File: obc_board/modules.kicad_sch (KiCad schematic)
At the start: 26 parts, among them J1 FSI-110-03-X-D-AD-SD-K-TR, J2 FSI-110-03-X-D-AD-SD-K-TR, U12 LTC4304IMS#PBF, U13 LTC4304IMS#PBF

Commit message: updated pcb
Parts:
- FL1, FL2: footprint FIL_PLT5BPH1015R6SNL -> cubesat_obc:FIL_PLT5BPH1015R6SNL
- J1, J2: footprint SAMTEC_FSI-110-03-X-D-AD-SD-K-TR -> cubesat_obc:SAMTEC_FSI-110-10-X-D-AD-TR
- U12, U13: footprint MSOP-10_MS -> Package_SO:MSOP-10_3x3mm_P0.5mm
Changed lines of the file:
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@@
     (property "Reference" "J1" (id 0) (at 115.57 56.7182 0))
     (property "Value" "FSI-110-03-X-D-AD-SD-K-TR" (id 1) (at 115.57 59.0296 0))
-    (property "Footprint" "SAMTEC_FSI-110-03-X-D-AD-SD-K-TR" (id 2) (at 115.57 76.2 0)
+    (property "Footprint" "cubesat_obc:SAMTEC_FSI-110-10-X-D-AD-TR" (id 2) (at 115.57 76.2 0)
       (effects (font (size 1.27 1.27)) (justify left bottom) hide)
     )
@@
     (property "Reference" "FL1" (id 0) (at 68.58 52.9082 0))
     (property "Value" "PLT5BPH1015R6SNL" (id 1) (at 68.58 55.2196 0))
-    (property "Footprint" "FIL_PLT5BPH1015R6SNL" (id 2) (at 68.58 63.5 0)
+    (property "Footprint" "cubesat_obc:FIL_PLT5BPH1015R6SNL" (id 2) (at 68.58 63.5 0)
       (effects (font (size 1.27 1.27)) (justify left bottom) hide)
     )
@@
     (property "Reference" "U12" (id 0) (at 93.98 98.6282 0))
     (property "Value" "LTC4304IMS#PBF" (id 1) (at 93.98 100.9396 0))
-    (property "Footprint" "MSOP-10_MS" (id 2) (at 78.74 105.41 0)
+    (property "Footprint" "Package_SO:MSOP-10_3x3mm_P0.5mm" (id 2) (at 78.74 105.41 0)
       (effects (font (size 1.27 1.27)) (justify left bottom) hide)
     )
@@
     (property "Reference" "J2" (id 0) (at 224.79 56.7182 0))
     (property "Value" "FSI-110-03-X-D-AD-SD-K-TR" (id 1) (at 224.79 59.0296 0))
-    (property "Footprint" "SAMTEC_FSI-110-03-X-D-AD-SD-K-TR" (id 2) (at 224.79 76.2 0)
+    (property "Footprint" "cubesat_obc:SAMTEC_FSI-110-10-X-D-AD-TR" (id 2) (at 224.79 76.2 0)
       (effects (font (size 1.27 1.27)) (justify left bottom) hide)
     )
@@
     (property "Reference" "FL2" (id 0) (at 177.8 52.9082 0))
     (property "Value" "PLT5BPH1015R6SNL" (id 1) (at 177.8 55.2196 0))
-    (property "Footprint" "FIL_PLT5BPH1015R6SNL" (id 2) (at 177.8 63.5 0)
+    (property "Footprint" "cubesat_obc:FIL_PLT5BPH1015R6SNL" (id 2) (at 177.8 63.5 0)
       (effects (font (size 1.27 1.27)) (justify left bottom) hide)
     )
@@
     (property "Reference" "U13" (id 0) (at 203.2 98.6282 0))
     (property "Value" "LTC4304IMS#PBF" (id 1) (at 203.2 100.9396 0))
-    (property "Footprint" "MSOP-10_MS" (id 2) (at 187.96 105.41 0)
-      (effects (font (size 1.27 1.27)) (justify left bottom) hide)
-    )
+    (property "Footprint" "Package_SO:MSOP-10_3x3mm_P0.5mm" (id 2) (at 187.96 105.41 0)
+      (effects (font (size 1.27 1.27)) (justify left bottom) hide)
+    )

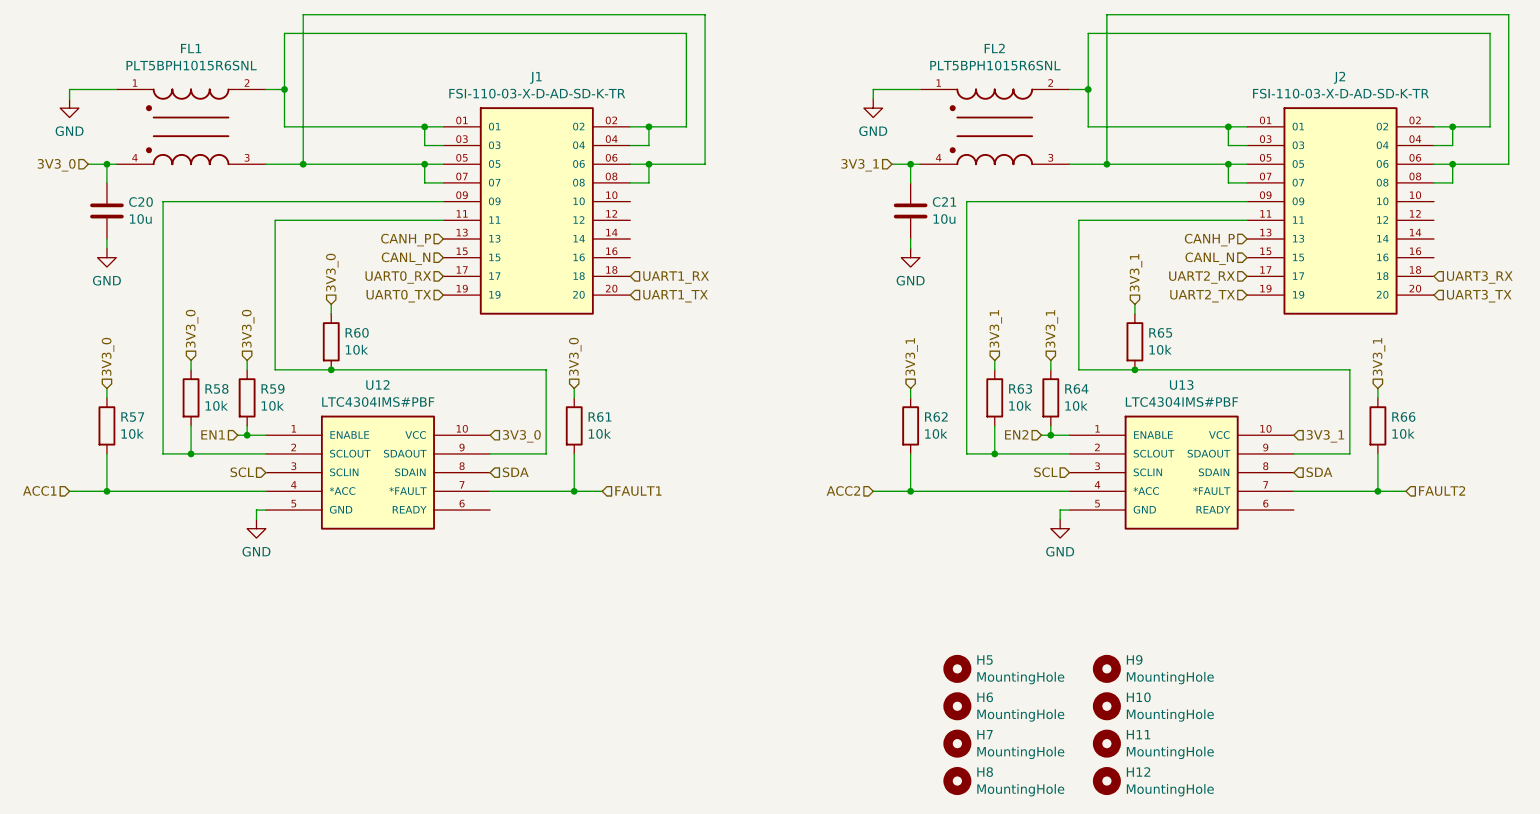
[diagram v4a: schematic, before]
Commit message: added silkscreen labels and gerber file
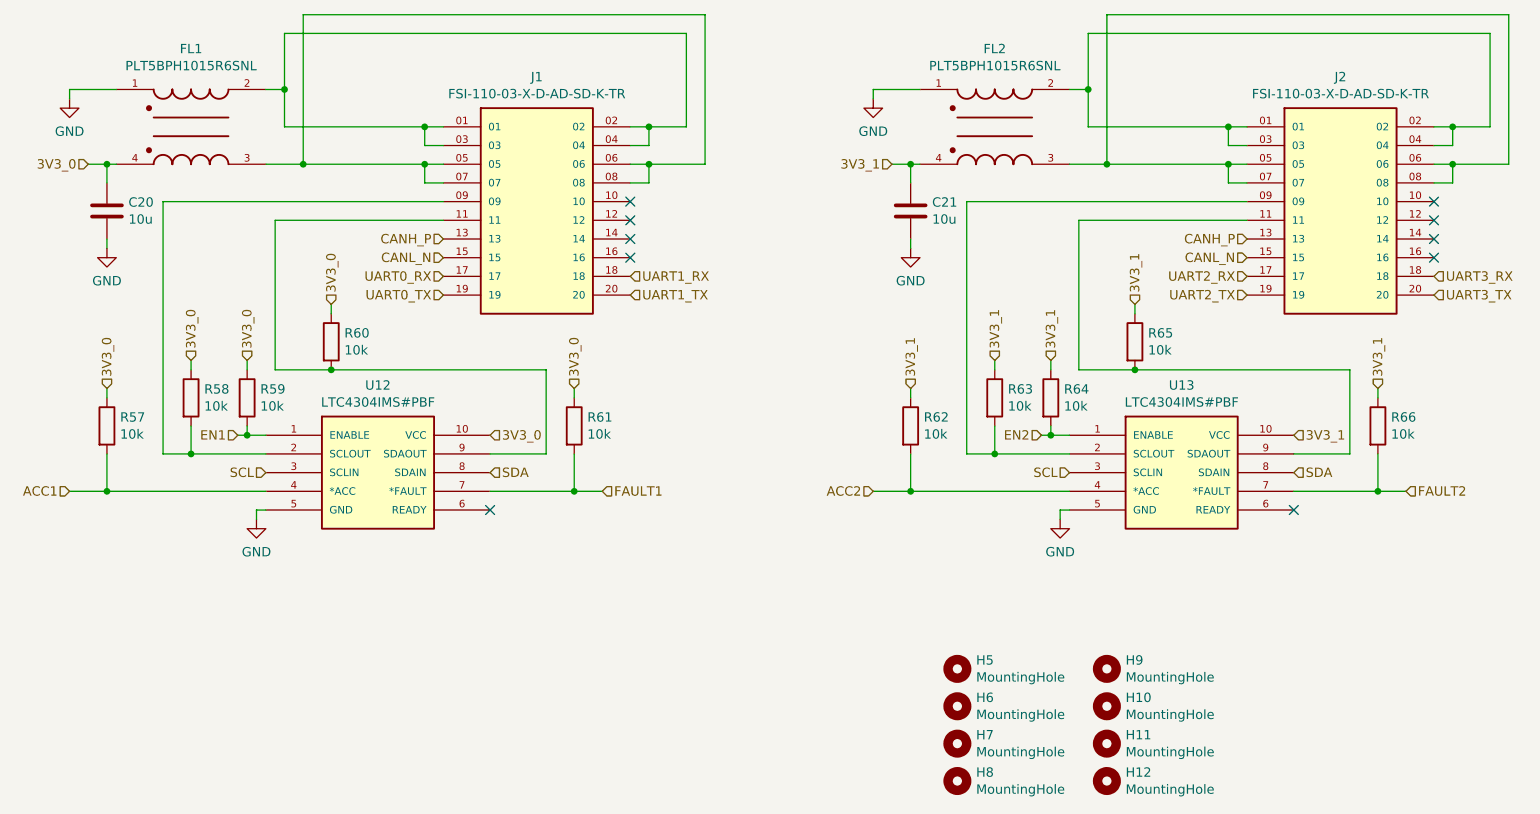
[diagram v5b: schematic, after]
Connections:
- no-connect marks 0 -> 10
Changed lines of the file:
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@@
   (junction (at 130.81 63.5) (diameter 0) (color 0 0 0 0)
   )
+  (no_connect (at 128.27 73.66))
+  (no_connect (at 237.49 73.66))
+  (no_connect (at 237.49 76.2))
+  (no_connect (at 237.49 78.74))
+  (no_connect (at 237.49 81.28))
+  (no_connect (at 218.44 115.57))
+  (no_connect (at 128.27 76.2))
+  (no_connect (at 128.27 78.74))
+  (no_connect (at 128.27 81.28))
+  (no_connect (at 109.22 115.57))
   (wire (pts (xy 68.58 104.14) (xy 68.58 107.95))
     (stroke (width 0) (type default) (color 0 0 0 0))
